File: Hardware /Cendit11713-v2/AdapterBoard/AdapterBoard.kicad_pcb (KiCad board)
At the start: 2 copper layers, 5 parts, among them J1 BOARD_EDGE_22P, J2 PIN_HEADER_01X22, J3 SLIMLINE_SATA_PLUG_7P_6P_HORZ, J4 SATA_RECEPTACLE_VERTICAL_SMT_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, J5 SATA_BACKPLANE_RECEPTACLE_VER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

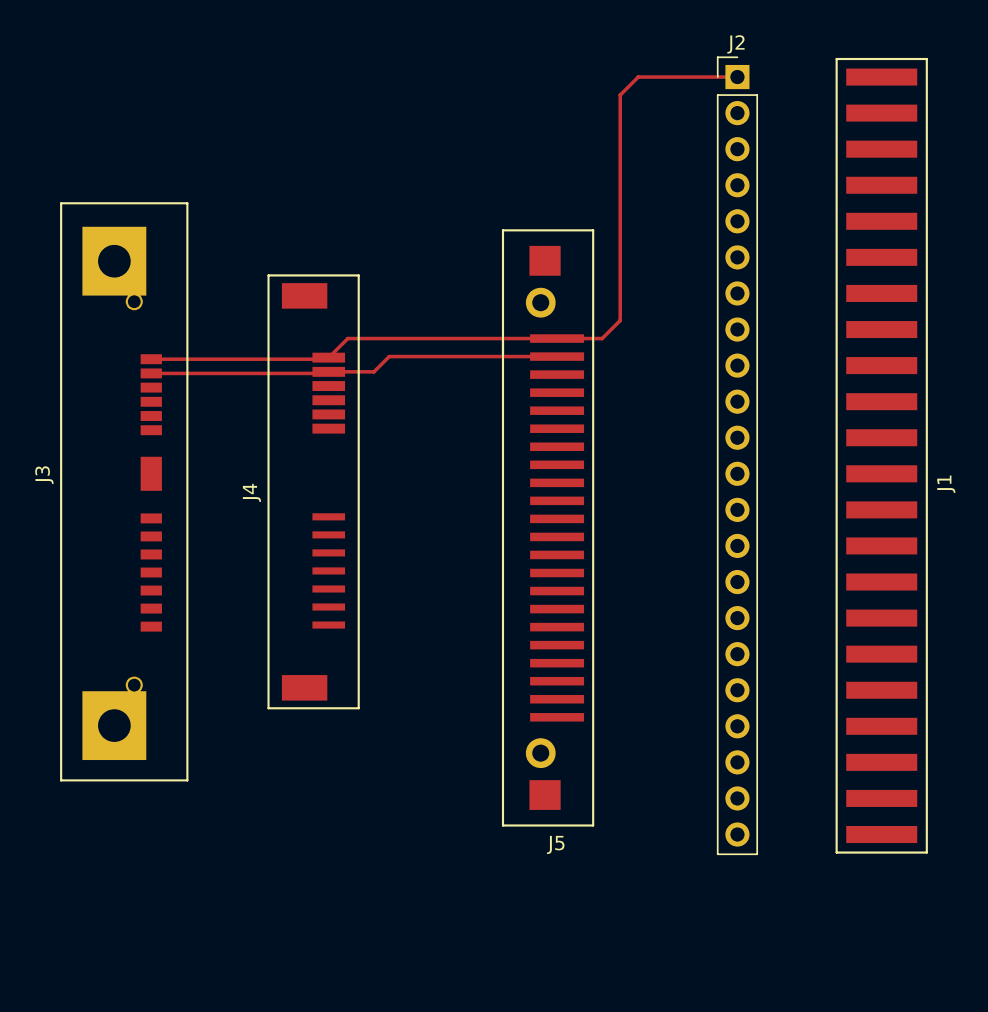
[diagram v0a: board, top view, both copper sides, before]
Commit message: Trabajo en CenditLab.Reducido + Cendit17713 PCB
  - Clases paneles UI modificados
  - Clases para manejo y validacion de datos
  - PCB expansor puertos Viking
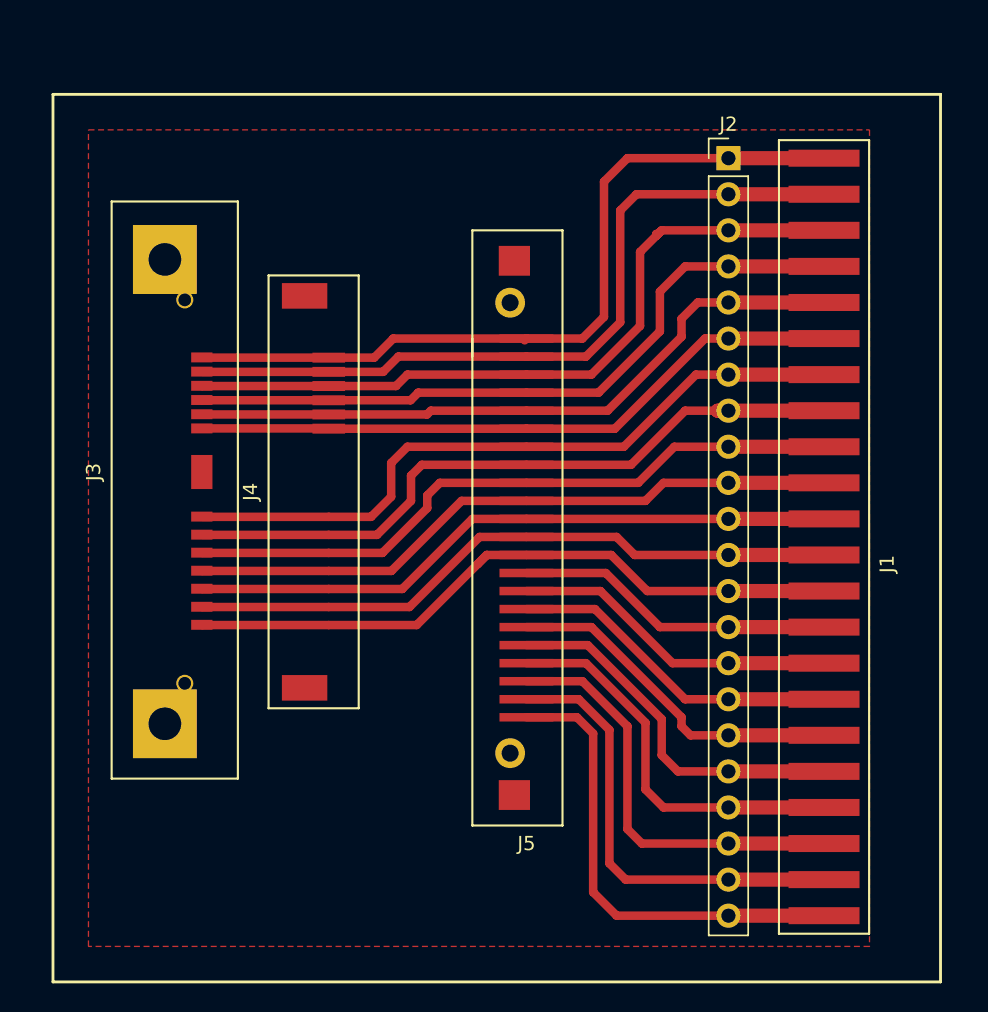
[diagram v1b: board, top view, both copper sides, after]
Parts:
- moved J1 7.01 mm to (209.3, 112.4)
- moved J2 5.75 mm to (202.6, 87.0)
- moved J3 3.56 mm to (165.5, 109.1)
- moved J5 2.16 mm to (185.8, 99.7)
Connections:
- net /23 renamed GND
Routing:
- net /3: track 0.00 -> 52.0 mm
- net /8: track 0.00 -> 50.0 mm
- net /7: track 0.00 -> 49.4 mm
- net /4: track 0.00 -> 49.4 mm
- net /5: track 0.00 -> 47.8 mm
- net /13: track 0.00 -> 47.8 mm
- net /9: track 0.00 -> 47.4 mm
- net /6: track 0.00 -> 46.5 mm
- net /10: track 0.00 -> 46.4 mm
- net /12: track 0.00 -> 46.4 mm
- net /11: track 0.00 -> 45.9 mm
- net /22: track 0.00 -> 33.3 mm
- net /21: track 0.00 -> 31.7 mm
- net /20: track 0.00 -> 29.9 mm
- net /19: track 0.00 -> 27.9 mm
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- added copper zone on F.Cu, net GND

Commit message: Trabajo en Cendit11713
  - Revision de esquematicos + PCBs
  - Generacion de archivos Gerber
  - CapacitiveKeyboard -> edicion PCB
  - Inicia PCB GpibPortExpander
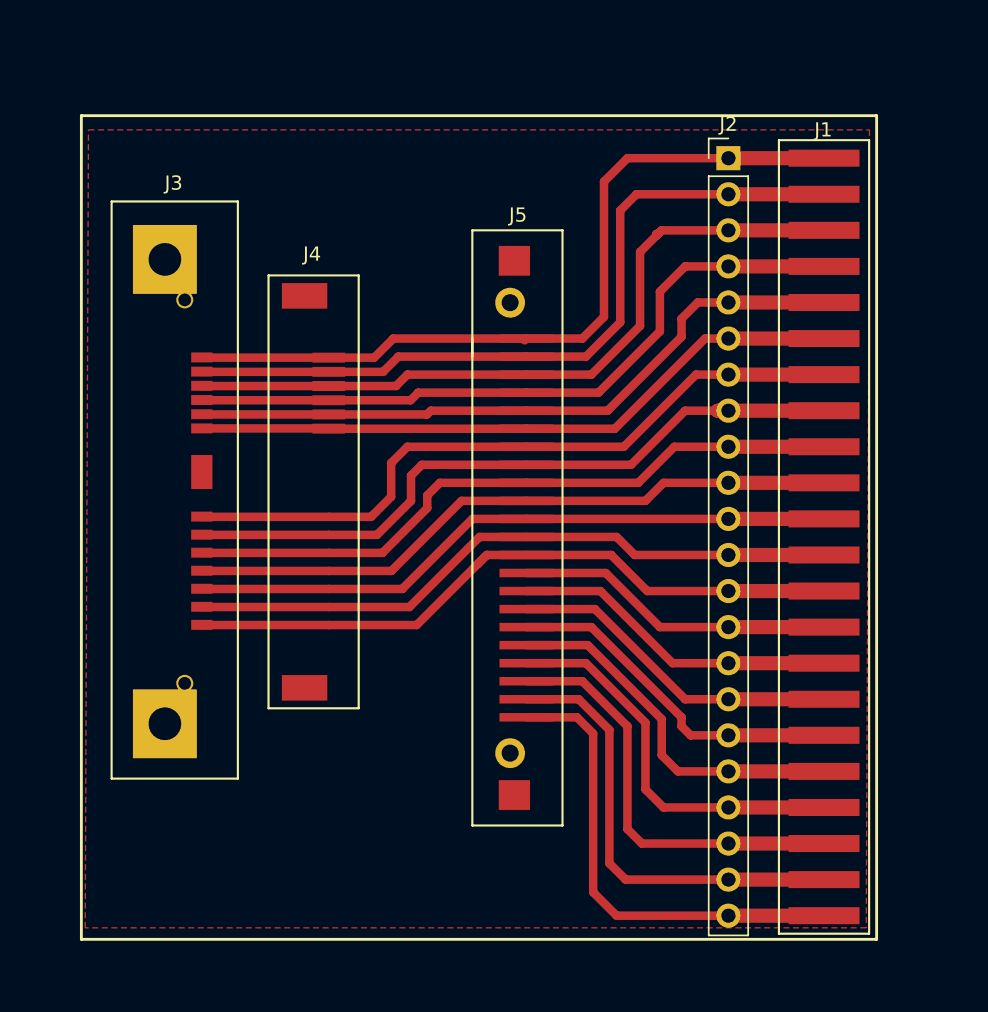
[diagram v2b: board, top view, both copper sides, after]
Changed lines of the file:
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@@
     (links 75)
     (no_connects 4)
-    (area 154.899999 82.399999 217.600001 145.100001)
+    (area 154.899999 82.399999 233.148045 155.987513)
     (thickness 1.6)
-    (drawings 6)
+    (drawings 7)
     (tracks 189)
     (zones 0)
@@
   )
   (setup
-    (last_trace_width 0.6)
+    (last_trace_width 1)
     (user_trace_width 0.3)
+    (user_trace_width 0.5)
     (user_trace_width 0.6)
     (user_trace_width 1)
+    (user_trace_width 2)
+    (user_trace_width 3)
+    (user_trace_width 4)
+    (user_trace_width 5)
     (trace_clearance 0.2)
-    (zone_clearance 0.6)
-    (zone_45_only no)
+    (zone_clearance 1)
+    (zone_45_only yes)
     (trace_min 0.2)
     (segment_width 0.2)
@@
     (at 209.296 112.395 270)
     (descr 20)
-    (fp_text reference J1 (at 3.175 -4.445 270) (layer F.SilkS)
-      (effects (font (size 1 1) (thickness 0.15)))
-    )
-    (fp_text value BOARD_EDGE_22P (at 2.54 4.445 270) (layer F.Fab)
+    (fp_text reference J1 (at -27.395 0.046 360) (layer F.SilkS)
+      (effects (font (size 1 1) (thickness 0.15)))
+    )
+    (fp_text value BOARD_EDGE_22P (at 0.605 4.296 270) (layer F.Fab)
       (effects (font (size 1 1) (thickness 0.15)))
     )
@@
       (effects (font (size 1 1) (thickness 0.15)))
     )
-    (fp_text value PIN_HEADER_01X22 (at 0 55.73) (layer F.Fab)
+    (fp_text value PIN_HEADER_01X22 (at -2.565 28.005 90) (layer F.Fab)
       (effects (font (size 1 1) (thickness 0.15)))
     )
@@
   (module CenditFootprints:SLIMLINE_SATA_PLUG_7P_6P (layer F.Cu)
     (at 165.481 109.093 270)
-    (fp_text reference J3 (at 0 7.62 270) (layer F.SilkS)
+    (fp_text reference J3 (at -20.343 1.981 360) (layer F.SilkS)
       (effects (font (size 1 1) (thickness 0.15)))
     )
@@
     (at 172.72 110.49 270)
     (descr 3)
-    (fp_text reference J4 (at 0 3.81 270) (layer F.SilkS)
+    (fp_text reference J4 (at -16.74 -0.53 360) (layer F.SilkS)
       (effects (font (size 1 1) (thickness 0.15)))
     )
@@
     (at 185.801 99.695)
     (descr 21)
-    (fp_text reference J5 (at 2.54 35.56) (layer F.SilkS)
+    (fp_text reference J5 (at 1.949 -8.695) (layer F.SilkS)
       (effects (font (size 1 1) (thickness 0.15)))
     )
@@
       (net 23 GND))
   )
-  (dimension 55.245146 (width 0.3) (layer F.SilkS)
-    (gr_text 55,245mm (at 185.49565 154.574015 0.1317142036) (layer F.SilkS)
+  (dimension 56.500553 (width 0.3) (layer F.SilkS)
+    (gr_text 56,501mm (at 220.974928 113.269247 89.74648051) (layer F.SilkS)
       (effects (font (size 1.5 1.5) (thickness 0.3)))
     )
-    (feature1 (pts (xy 213.106 149.225) (xy 213.121254 155.860512)))
-    (feature2 (pts (xy 157.861 149.352) (xy 157.876254 155.987512)))
-    (crossbar (pts (xy 157.870047 153.287519) (xy 213.115047 153.160519)))
-    (arrow1a (pts (xy 213.115047 153.160519) (xy 211.989894 153.749528)))
-    (arrow1b (pts (xy 213.115047 153.160519) (xy 211.987198 152.576689)))
-    (arrow2a (pts (xy 157.870047 153.287519) (xy 158.997896 153.871349)))
-    (arrow2b (pts (xy 157.870047 153.287519) (xy 158.9952 152.69851)))
-  )
-  (dimension 58.166139 (width 0.3) (layer F.SilkS)
-    (gr_text 58,166mm (at 227.219473 114.059761 89.87490024) (layer F.SilkS)
+    (feature1 (pts (xy 216.5 141.5) (xy 222.199915 141.525221)))
+    (feature2 (pts (xy 216.75 85) (xy 222.449915 85.025221)))
+    (crossbar (pts (xy 219.749941 85.013274) (xy 219.499941 141.513274)))
+    (arrow1a (pts (xy 219.499941 141.513274) (xy 218.91851 140.384187)))
+    (arrow1b (pts (xy 219.499941 141.513274) (xy 220.09134 140.389376)))
+    (arrow2a (pts (xy 219.749941 85.013274) (xy 219.158542 86.137172)))
+    (arrow2b (pts (xy 219.749941 85.013274) (xy 220.331372 86.142361)))
+  )
+  (dimension 54.5 (width 0.3) (layer F.SilkS)
+    (gr_text 54,500mm (at 184.75 76.15) (layer F.SilkS)
       (effects (font (size 1.5 1.5) (thickness 0.3)))
     )
-    (feature1 (pts (xy 220.853 143.129) (xy 228.50597 143.145709)))
-    (feature2 (pts (xy 220.98 84.963) (xy 228.63297 84.979709)))
-    (crossbar (pts (xy 225.932976 84.973814) (xy 225.805976 143.139814)))
-    (arrow1a (pts (xy 225.805976 143.139814) (xy 225.222016 142.012033)))
-    (arrow1b (pts (xy 225.805976 143.139814) (xy 226.394855 142.014593)))
-    (arrow2a (pts (xy 225.932976 84.973814) (xy 225.344097 86.099035)))
-    (arrow2b (pts (xy 225.932976 84.973814) (xy 226.516936 86.101595)))
-  )
-  (gr_line (start 155 82.5) (end 217.5 82.5) (angle 90) (layer F.SilkS) (width 0.2))
-  (gr_line (start 155 145) (end 155 82.5) (angle 90) (layer F.SilkS) (width 0.2))
-  (gr_line (start 217.5 145) (end 155 145) (angle 90) (layer F.SilkS) (width 0.2))
-  (gr_line (start 217.5 82.5) (end 217.5 145) (angle 90) (layer F.SilkS) (width 0.2))
+    (feature1 (pts (xy 212 80.75) (xy 212 74.8)))
+    (feature2 (pts (xy 157.5 80.75) (xy 157.5 74.8)))
+    (crossbar (pts (xy 157.5 77.5) (xy 212 77.5)))
+    (arrow1a (pts (xy 212 77.5) (xy 210.873496 78.086421)))
+    (arrow1b (pts (xy 212 77.5) (xy 210.873496 76.913579)))
+    (arrow2a (pts (xy 157.5 77.5) (xy 158.626504 78.086421)))
+    (arrow2b (pts (xy 157.5 77.5) (xy 158.626504 76.913579)))
+  )
+  (target plus (at 157.25 141.25) (size 5) (width 0.15) (layer Edge.Cuts))
+  (gr_line (start 213 142) (end 213 84) (angle 90) (layer F.SilkS) (width 0.2))
+  (gr_line (start 157 142) (end 213 142) (angle 90) (layer F.SilkS) (width 0.2))
+  (gr_line (start 157 84) (end 157 142) (angle 90) (layer F.SilkS) (width 0.2))
+  (gr_line (start 213 84) (end 157 84) (angle 90) (layer F.SilkS) (width 0.2))
   (segment (start 209.296 86.995) (end 202.565 86.995) (width 1) (layer F.Cu) (net 1))
   (segment (start 174.42 101.04) (end 165.498 101.04) (width 0.6) (layer F.Cu) (net 1))
@@
   (segment (start 191.897 126.365) (end 188.341 126.365) (width 0.6) (layer F.Cu) (net 22))
   (zone (net 23) (net_name GND) (layer F.Cu) (hatch edge 0.508)
-    (connect_pads (clearance 0.6))
+    (connect_pads (clearance 1))
     (min_thickness 0.254)
     (fill yes (arc_segments 16) (thermal_gap 1) (thermal_bridge_width 1))
     (polygon
       (pts
-        (xy 212.5 142.5) (xy 157.5 142.5) (xy 157.5 85) (xy 212.5 85)
+        (xy 212.27 141.19) (xy 157.27 141.19) (xy 157.5 85) (xy 212.5 85)
       )
     )
